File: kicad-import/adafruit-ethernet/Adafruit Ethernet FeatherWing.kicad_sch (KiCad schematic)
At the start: 47 parts, among them IC2 74AHC1G125, X3 RB1-125BAG1A, Y1 25MHz

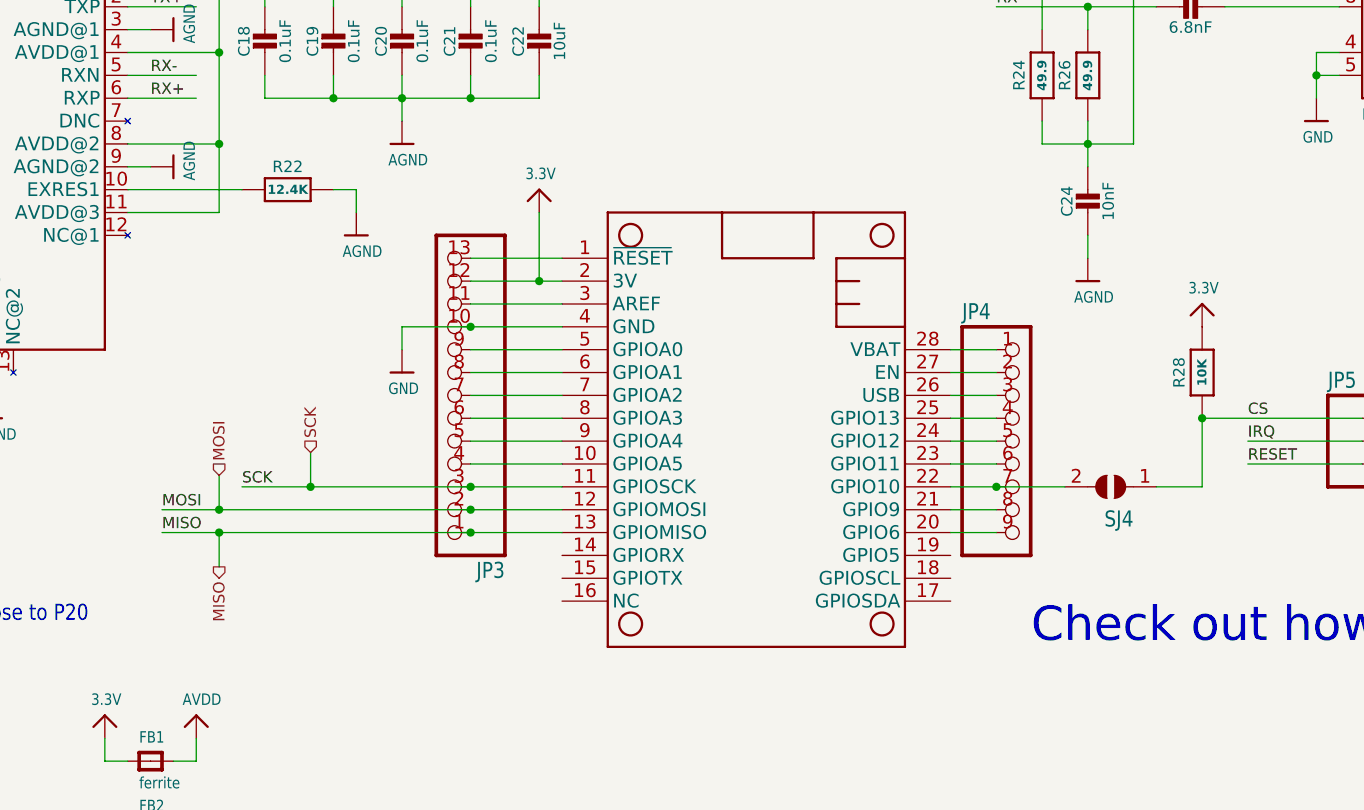
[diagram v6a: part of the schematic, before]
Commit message: Improve sheet labels. Remove extra model and headers from ETH and RTC pages.
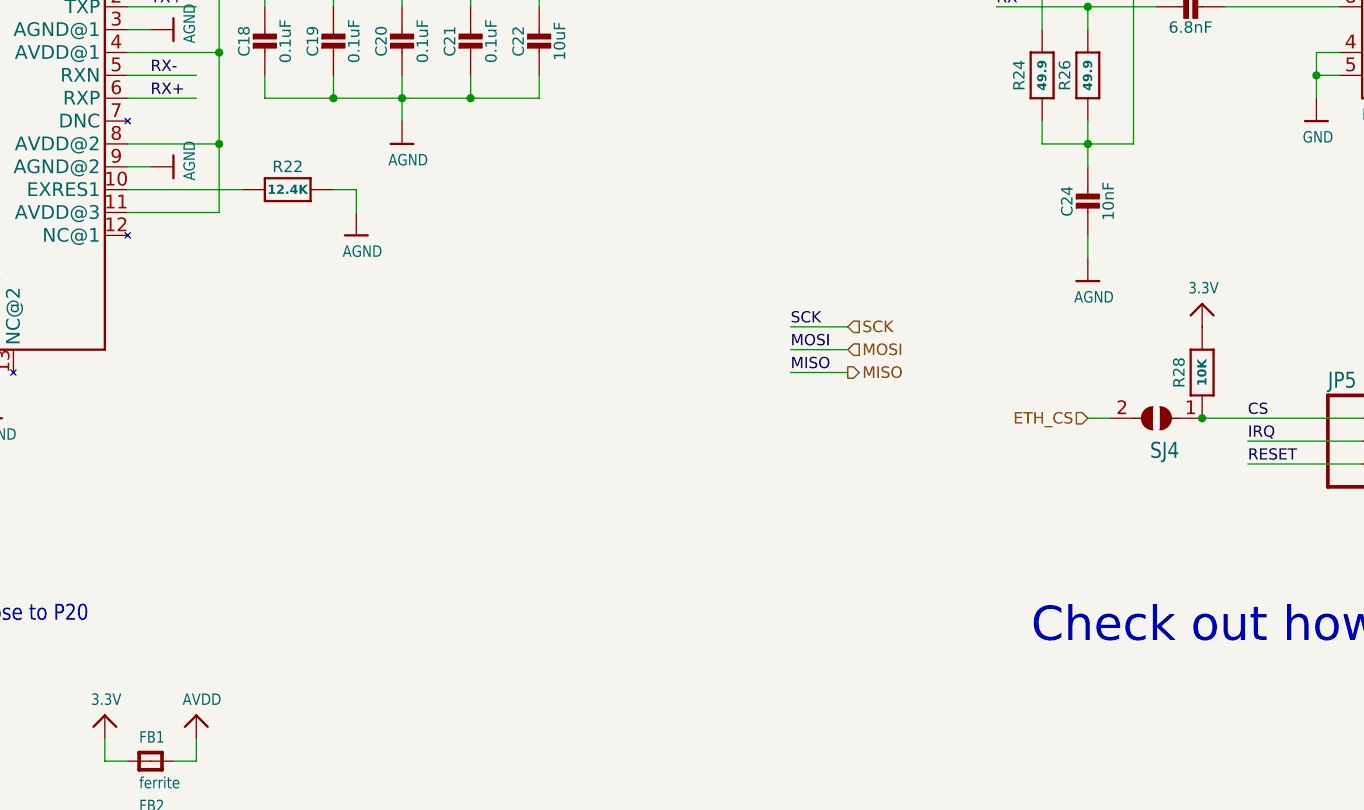
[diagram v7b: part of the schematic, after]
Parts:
- removed JP3: HEADER-1X13, Adafruit Ethernet FeatherWing:1X13_ROUND_70, symbol Adafruit Ethernet FeatherWing-eagle-import:HEADER-1X13
- removed JP4: HEADER-1X970MIL, Adafruit Ethernet FeatherWing:1X09_ROUND_70, symbol Adafruit Ethernet FeatherWing-eagle-import:HEADER-1X970MIL
- removed MS1: FEATHERWING_NODIM, Adafruit Ethernet FeatherWing:FEATHERWING_NODIM, symbol Adafruit Ethernet FeatherWing-eagle-import:FEATHERWING_NODIM
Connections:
- net ETH_CS: now reaches SJ4.2
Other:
- moved on the sheet: SJ4

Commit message: Some more net and label cleanup.
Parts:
- renumbered U$5 to U2
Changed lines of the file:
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@@
 	(wire
 		(pts
-			(xy 60.96 172.72) (xy 73.66 172.72)
+			(xy 60.96 172.72) (xy 67.31 172.72)
 		)
 		(stroke
@@
 	(wire
 		(pts
-			(xy 190.5 114.3) (xy 196.85 114.3)
-		)
-		(stroke
-			(width 0.1524)
-			(type solid)
-		)
-	)
-	(wire
-		(pts
 			(xy 226.06 124.46) (xy 223.52 124.46)
 		)
@@
 	(wire
 		(pts
-			(xy 190.5 119.38) (xy 196.85 119.38)
-		)
-		(stroke
-			(width 0.1524)
-			(type solid)
-		)
-	)
-	(wire
-		(pts
 			(xy 45.72 96.52) (xy 45.72 127)
 		)
@@
 	(wire
 		(pts
-			(xy 190.5 116.84) (xy 196.85 116.84)
-		)
-		(stroke
-			(width 0.1524)
-			(type solid)
-		)
-	)
-	(wire
-		(pts
 			(xy 96.52 58.42) (xy 96.52 50.8)
 		)
@@
 	)
 	(label "MISO"
-		(at 190.5 119.38 0)
-		(effects
-			(font
-				(size 1.2446 1.2446)
-			)
-			(justify left bottom)
-		)
-	)
-	(label "MISO"
 		(at 60.96 172.72 0)
 		(effects
@@
 		)
 	)
-	(label "MOSI"
-		(at 190.5 116.84 0)
-		(effects
-			(font
-				(size 1.2446 1.2446)
-			)
-			(justify left bottom)
-		)
-	)
 	(label "RX+"
 		(at 213.36 73.66 0)
@@
 		)
 	)
-	(label "SCK"
-		(at 190.5 114.3 0)
-		(effects
-			(font
-				(size 1.2446 1.2446)
-			)
-			(justify left bottom)
-		)
-	)
 	(label "CS"
 		(at 30.48 162.56 0)
@@
 		)
 	)
-	(hierarchical_label "ETH_CS"
+	(hierarchical_label "MOSI"
 		(shape input)
-		(at 223.52 124.46 180)
+		(at 50.8 78.74 180)
 		(effects
 			(font
@@
 		)
 	)
-	(hierarchical_label "MISO"
-		(shape output)
-		(at 196.85 119.38 0)
+	(hierarchical_label "ETH_CS"
+		(shape input)
+		(at 223.52 124.46 180)
 		(effects
 			(font
 				(size 1.27 1.27)
 			)
-			(justify left)
+			(justify right)
 		)
 	)
-	(hierarchical_label "MOSI"
-		(shape input)
-		(at 196.85 116.84 0)
+	(hierarchical_label "MISO"
+		(shape output)
+		(at 67.31 172.72 0)
 		(effects
 			(font
@@
 	(hierarchical_label "SCK"
 		(shape input)
-		(at 196.85 114.3 0)
+		(at 50.8 83.82 180)
 		(effects
 			(font
 				(size 1.27 1.27)
 			)
-			(justify left)
+			(justify right)
 		)
 	)
@@
 		(on_board yes)
 		(dnp no)
-		(property "Reference" "U$5"
+		(property "Reference" "U2"
 			(at 63.5 58.42 0)
 			(effects
@@
 			(project "Genesis"
 				(path "/66b8af00-4ede-44e3-a762-88857219665d/34668455-eab9-44a0-a7b2-48f3dfe2249d"
-					(reference "U$5")
+					(reference "U2")
 					(unit 1)
 				)
